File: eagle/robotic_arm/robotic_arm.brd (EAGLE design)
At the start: 160 x 100 mm, 0 parts

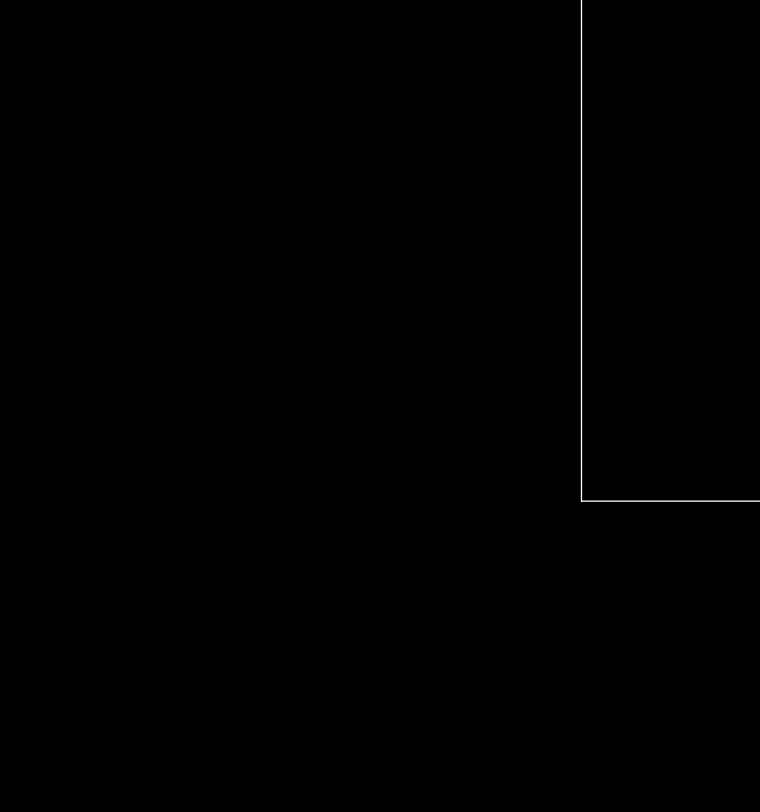
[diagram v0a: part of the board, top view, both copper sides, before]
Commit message: Added PWM driver and DEMUX to both robotic arm and touch glove.  Added some transistors to touch glove
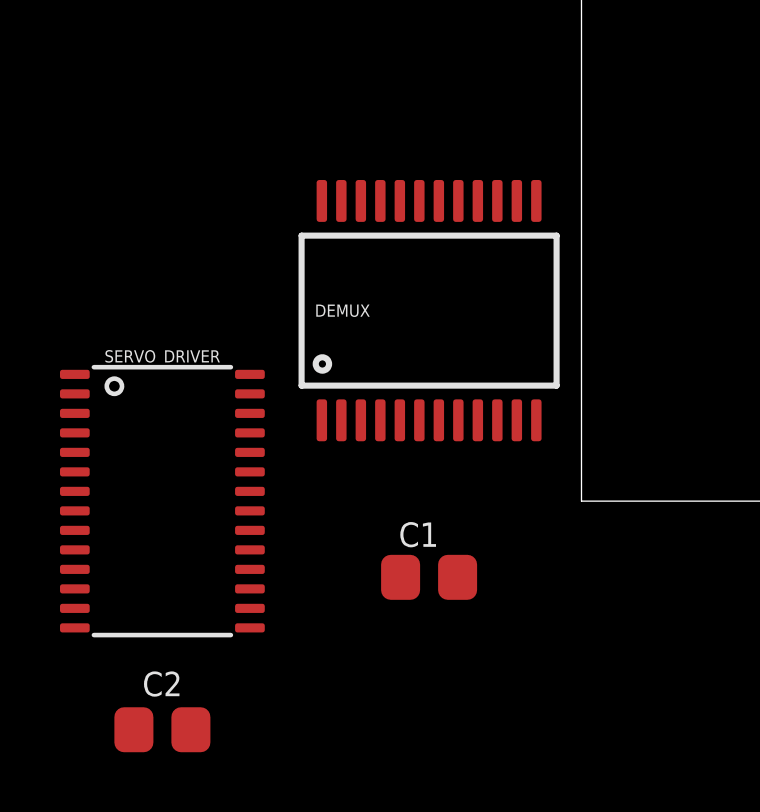
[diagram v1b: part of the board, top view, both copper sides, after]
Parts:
- added C1: CAP_CER_SMD-805_0.1UF-50V-10%, MrSwirlyEyes:CAP_CER_SMD-805_0.1UF-50V-10%
- added C2: CAP_CER_SMD-805_10UF-25V-10%, MrSwirlyEyes:CAP_CER_SMD-805_10UF-25V-10%
- added DEMUX: CD74HCT4067_16-CH_MUX-DEMUX, MrSwirlyEyes:SSOP24
- added SERVO_DRIVER: PCA9685_16-CH_12-BIT_PWM-DRIVER, MrSwirlyEyes:TSSOP28
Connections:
- new net C10: DEMUX.22
- new net C5: DEMUX.4
- new net C6: DEMUX.3
- new net C7: DEMUX.2
- new net C8: DEMUX.23
- new net FORCE_1: DEMUX.9
- new net FORCE_2: DEMUX.8
- new net FORCE_3: DEMUX.7
- new net FORCE_4: DEMUX.6
- new net FORCE_5: DEMUX.5
- new net GND: C1.2, C2.2, DEMUX.12, DEMUX.15, SERVO_DRIVER.1, SERVO_DRIVER.14, SERVO_DRIVER.2, SERVO_DRIVER.23, SERVO_DRIVER.24, SERVO_DRIVER.25, SERVO_DRIVER.3, SERVO_DRIVER.4, SERVO_DRIVER.5
- new net N$16: DEMUX.21
- new net N$19: SERVO_DRIVER.11
- new net N$20: SERVO_DRIVER.12
- new net N$21: SERVO_DRIVER.13
- new net N$22: SERVO_DRIVER.15
- new net N$23: SERVO_DRIVER.16
- new net N$24: SERVO_DRIVER.17
- new net N$25: SERVO_DRIVER.18
- new net N$26: SERVO_DRIVER.19
- new net N$27: SERVO_DRIVER.20
- new net N$28: SERVO_DRIVER.21
- new net N$29: SERVO_DRIVER.22
- new net S0: DEMUX.10
- new net S1: DEMUX.11
- new net S2: DEMUX.14
- new net S3: DEMUX.13
- new net SCL: SERVO_DRIVER.26
- new net SDA: SERVO_DRIVER.27
- new net SERVO_INDEX: SERVO_DRIVER.9
- new net SERVO_MIDDLE: SERVO_DRIVER.8
- new net SERVO_PINKY: SERVO_DRIVER.6
- new net SERVO_RING: SERVO_DRIVER.7
- new net SERVO_THUMB: SERVO_DRIVER.10
- new net SIG: DEMUX.1
- new net TEMP_1: DEMUX.20
- new net TEMP_2: DEMUX.19
- new net TEMP_3: DEMUX.18
- new net TEMP_4: DEMUX.17
- new net TEMP_5: DEMUX.16
- new net VCC: C1.1, C2.1, DEMUX.24, SERVO_DRIVER.28

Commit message: Added vibe motor plus transistor driver arrangement
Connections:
- net N$19 renamed PWM5
- net N$20 renamed PWM6
- net N$21 renamed PWM7
- net N$22 renamed PWM8
- net N$23 renamed PWM9
- net N$24 renamed PWM10
- net N$25 renamed PWM11
- net N$26 renamed PWM12
- net N$27 renamed PWM13
- net N$28 renamed PWM14
- net N$29 renamed PWM15
- removed net N$16: DEMUX.21
- new net C9: DEMUX.22
- net C10: now also DEMUX.21; no longer DEMUX.22
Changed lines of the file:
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@@
 <contactref element="DEMUX" pad="23"/>
 </signal>
-<signal name="C10">
+<signal name="C9">
 <contactref element="DEMUX" pad="22"/>
 </signal>
-<signal name="N$16">
+<signal name="C10">
 <contactref element="DEMUX" pad="21"/>
 </signal>
@@
 <contactref element="SERVO_DRIVER" pad="10"/>
 </signal>
-<signal name="N$19">
+<signal name="PWM5">
 <contactref element="SERVO_DRIVER" pad="11"/>
 </signal>
-<signal name="N$20">
+<signal name="PWM6">
 <contactref element="SERVO_DRIVER" pad="12"/>
 </signal>
-<signal name="N$21">
+<signal name="PWM7">
 <contactref element="SERVO_DRIVER" pad="13"/>
 </signal>
-<signal name="N$22">
+<signal name="PWM8">
 <contactref element="SERVO_DRIVER" pad="15"/>
 </signal>
-<signal name="N$23">
+<signal name="PWM9">
 <contactref element="SERVO_DRIVER" pad="16"/>
 </signal>
-<signal name="N$24">
+<signal name="PWM10">
 <contactref element="SERVO_DRIVER" pad="17"/>
 </signal>
-<signal name="N$25">
+<signal name="PWM11">
 <contactref element="SERVO_DRIVER" pad="18"/>
 </signal>
-<signal name="N$26">
+<signal name="PWM12">
 <contactref element="SERVO_DRIVER" pad="19"/>
 </signal>
-<signal name="N$27">
+<signal name="PWM13">
 <contactref element="SERVO_DRIVER" pad="20"/>
 </signal>
-<signal name="N$28">
+<signal name="PWM14">
 <contactref element="SERVO_DRIVER" pad="21"/>
 </signal>
-<signal name="N$29">
+<signal name="PWM15">
 <contactref element="SERVO_DRIVER" pad="22"/>
 </signal>

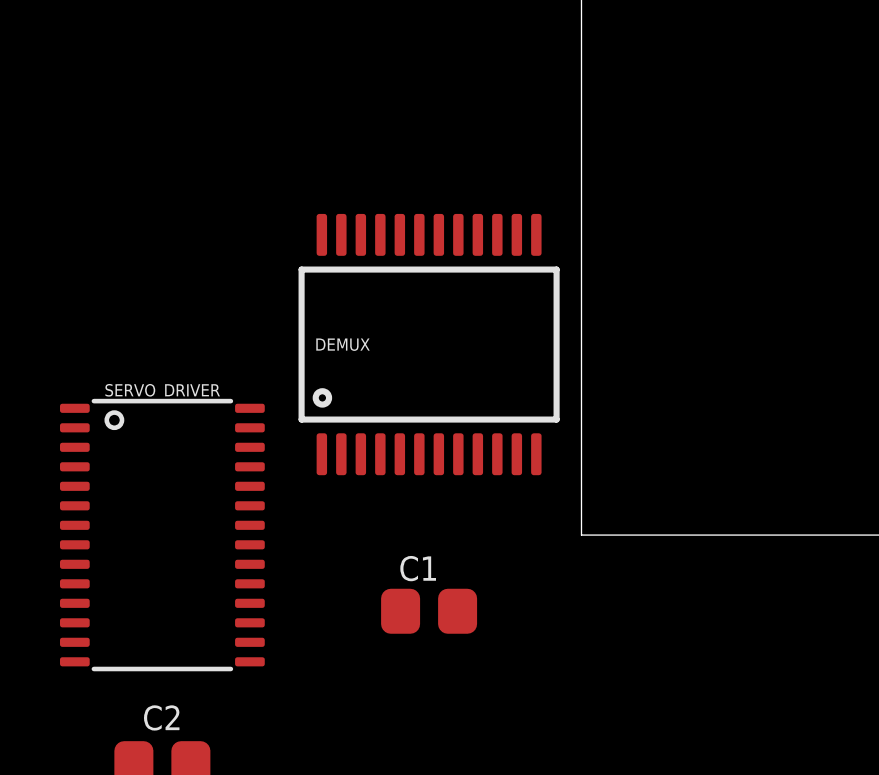
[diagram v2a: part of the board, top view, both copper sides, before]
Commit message: Added Peltier driving circuitry
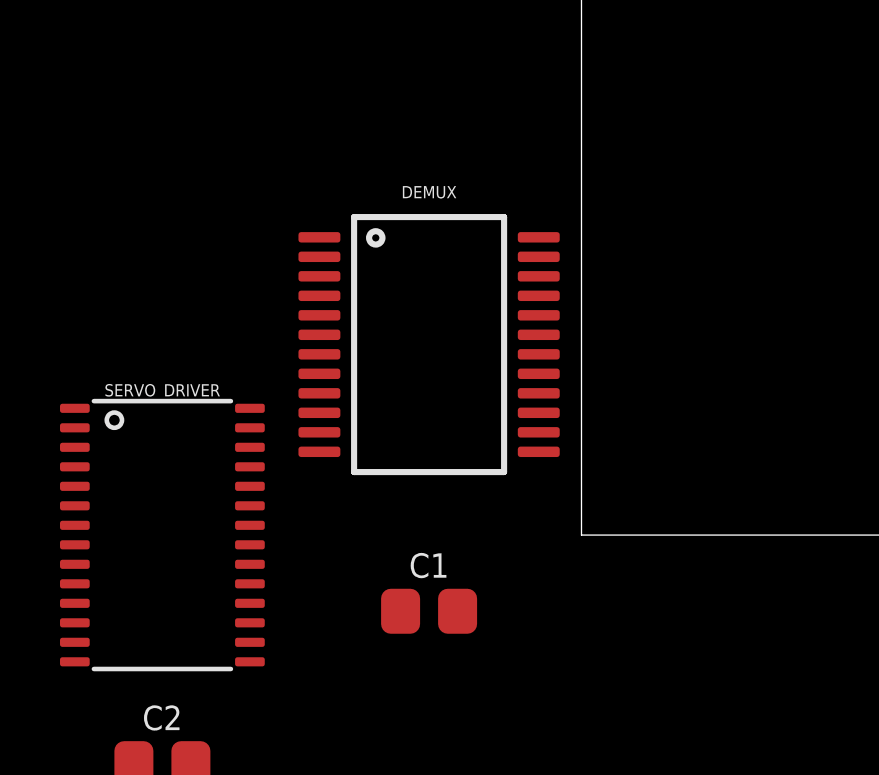
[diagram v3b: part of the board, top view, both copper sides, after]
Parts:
- DEMUX: value CD74HCT4067_16-CH_MUX-DEMUX -> CD74HC4067-SM96_16:1_MUX-DEMUX
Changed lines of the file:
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@@
 </autorouter>
 <elements>
-<element name="DEMUX" library="MrSwirlyEyes" package="SSOP24" value="CD74HCT4067_16-CH_MUX-DEMUX" x="-5.08" y="6.35">
+<element name="DEMUX" library="MrSwirlyEyes" package="SSOP24" value="CD74HC4067-SM96_16:1_MUX-DEMUX" x="-5.08" y="6.35">
 <attribute name="CREATOR" value="MrSwirlyEyes" x="-5.08" y="6.35" size="1.778" layer="27" display="off"/>
-<attribute name="DATASHEET" value="http://www.ti.com/lit/ds/symlink/cd74hct4067-q1.pdf" x="-5.08" y="6.35" size="1.778" layer="27" display="off"/>
+<attribute name="DATASHEET" value="http://www.ti.com/lit/ds/symlink/cd74hc4067.pdf" x="-5.08" y="6.35" size="1.778" layer="27" display="off"/>
 <attribute name="DIST" value="Digikey" x="-5.08" y="6.35" size="1.778" layer="27" display="off"/>
-<attribute name="DISTPN" value="296-37976-1-ND" x="-5.08" y="6.35" size="1.778" layer="27" display="off"/>
+<attribute name="DISTPN" value="296-9226-1-ND" x="-5.08" y="6.35" size="1.778" layer="27" display="off"/>
 <attribute name="MFR" value="Texas Instruments" x="-5.08" y="6.35" size="1.778" layer="27" display="off"/>
-<attribute name="MPN" value="CD74HCT4067QM96Q1" x="-5.08" y="6.35" size="1.778" layer="27" display="off"/>
+<attribute name="MPN" value="CD74HC4067SM96" x="-5.08" y="6.35" size="1.778" layer="27" display="off"/>
 <attribute name="TESTED" value="NO" x="-5.08" y="6.35" size="1.778" layer="27" display="off"/>
 </element>
@@
 <wire x1="-11.0522" y1="0.975" x2="-11.0522" y2="1.625" width="0" layer="19" extent="1-1"/>
 <wire x1="-4.13" y1="-2.54" x2="-11.0522" y2="0.975" width="0" layer="19" extent="1-1"/>
-<wire x1="-1.505" y1="2.694" x2="-4.13" y2="-2.54" width="0" layer="19" extent="1-1"/>
-<wire x1="-2.805" y1="10.006" x2="-1.505" y2="2.694" width="0" layer="19" extent="1-1"/>
+<wire x1="-8.736" y1="2.775" x2="-4.13" y2="-2.54" width="0" layer="19" extent="1-1"/>
+<wire x1="-1.424" y1="4.075" x2="-8.736" y2="2.775" width="0" layer="19" extent="1-1"/>
 </signal>
 <signal name="VCC">
@@
 <wire x1="-6.03" y1="-2.54" x2="-14.92" y2="-7.62" width="0" layer="19" extent="1-1"/>
 <wire x1="-11.0522" y1="4.225" x2="-6.03" y2="-2.54" width="0" layer="19" extent="1-1"/>
-<wire x1="-8.655" y1="10.006" x2="-11.0522" y2="4.225" width="0" layer="19" extent="1-1"/>
+<wire x1="-1.424" y1="9.925" x2="-11.0522" y2="4.225" width="0" layer="19" extent="1-1"/>
 </signal>
 <signal name="S0">

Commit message: Added FSR driver and servo driver for robotic arm
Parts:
- added A1, A2, A3, A4, A5: TMP36, MrSwirlyEyes:CONNECTOR_TMP36
- added C10, C12, C14, C16, C3, C4, C5, C6, C7, C8: CAP_CER_SMD-805_0.1UF-50V-10%, MrSwirlyEyes:CAP_CER_SMD-805_0.1UF-50V-10%
- added C11, C13, C15, C17, C9: CAP_POL_ALUM-ELECTROLYTIC_SMD_100UF-16V-20%, MrSwirlyEyes:CAP_POL_ALUM-ELECTROLYTIC_100UF-16V-20%_6.3LW-6.10H
- added F1, F2, F3, F4, F5: FSR, MrSwirlyEyes:CONNECTOR_FSR
- added R1, R2, R3, R4, R5: RES_SMD-805_10K-5%-1/8W, MrSwirlyEyes:RES_SMD-805_10K-5%-1/8W
- added S1, S2, S3, S4, S5: SERVO, MrSwirlyEyes:CONNECTOR_SERVO
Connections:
- net FORCE_1: now also F1.-, F2.-, F3.-, F4.-, F5.-, R1.2, R2.2, R3.2, R4.2, R5.2
- net GND: now also A1.3, A2.3, A3.3, A4.3, A5.3, C10.2, C11.K, C12.2, C13.K, C14.2, C15.K, C16.2, C17.K, C3.2, C4.2, C5.2, C6.2, C7.2, C8.2, C9.K, R1.1, R2.1, R3.1, R4.1, R5.1, S1.3, S2.3, S3.3, S4.3, S5.3
- net SERVO_INDEX: now also S4.1
- net SERVO_MIDDLE: now also S3.1
- net SERVO_PINKY: now also S1.1
- net SERVO_RING: now also S2.1
- net SERVO_THUMB: now also S5.1
- net TEMP_1: now also A1.2
- net TEMP_2: now also A2.2
- net TEMP_3: now also A3.2
- net TEMP_4: now also A4.2
- net TEMP_5: now also A5.2
- net VCC: now also A1.1, A2.1, A3.1, A4.1, A5.1, C10.1, C11.A, C12.1, C13.A, C14.1, C15.A, C16.1, C17.A, C3.1, C4.1, C5.1, C6.1, C7.1, C8.1, C9.A, F1.+, F2.+, F3.+, F4.+, F5.+, S1.2, S2.2, S3.2, S4.2, S5.2

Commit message: Modfied git ignore.  Added h bridge files.  Modified EAGLE files
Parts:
- C1, C10, C12, C14, C16, C3, C4, C5, C6, C7, C8: value CAP_CER_SMD-805_0.1UF-50V-10% -> 0.1uF/50V; device MrSwirlyEyes:CAP_CER_SMD-805_0.1UF-50V-10% -> MrSwirlyEyes:CAP_CER_SMD-805
- C11, C13, C15, C17, C9: value CAP_POL_ALUM-ELECTROLYTIC_SMD_100UF-16V-20% -> 100UF/16V; device MrSwirlyEyes:CAP_POL_ALUM-ELECTROLYTIC_100UF-16V-20%_6.3LW-6.10H -> MrSwirlyEyes:CAP_POL_ALUM-ELECTROLYTIC
- C2: value CAP_CER_SMD-805_10UF-25V-10% -> 10uF/25V; device MrSwirlyEyes:CAP_CER_SMD-805_10UF-25V-10% -> MrSwirlyEyes:CAP_CER_SMD-805
- DEMUX: value CD74HC4067-SM96_16:1_MUX-DEMUX -> CH16_MUX-DEMUX; device MrSwirlyEyes:SSOP24 -> MrSwirlyEyes:SSOP-24
- R1, R2, R3, R4, R5: value RES_SMD-805_10K-5%-1/8W -> 10KΩ; device MrSwirlyEyes:RES_SMD-805_10K-5%-1/8W -> MrSwirlyEyes:RESC2012X60_HS
- S1, S2, S3, S4, S5: value SERVO -> HK15298B
- SERVO_DRIVER: value PCA9685_16-CH_12-BIT_PWM-DRIVER -> PCA9685; device MrSwirlyEyes:TSSOP28 -> MrSwirlyEyes:TSSOP-28
- moved C7 271.5 mm to (-36.8, -405.1)
- moved F1 271.4 mm to (-29.2, -416.6)
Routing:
- net VCC: track 0.00 -> 31.5 mm

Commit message: Rev 1 of Robotic Arm schematic complete
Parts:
- removed DEMUX: CH16_MUX-DEMUX, MrSwirlyEyes:SSOP-24
- removed F1, F2, F3, F4, F5: FSR, MrSwirlyEyes:CONNECTOR_FSR
- removed R1, R2, R3, R4, R5: 10KΩ, MrSwirlyEyes:RESC2012X60_HS
- removed SERVO_DRIVER: PCA9685, MrSwirlyEyes:TSSOP-28
- added A6: ANTENNASMD5, lib_kenmei:ANTENNA-CHIP5
- added B1: 748421245, lib_kenmei:0805_BALUN
- added BATT1: BATTERYPTH_HOLES, MrSwirlyEyes:DUAL_PTH_PADS
- added C18, C25, C82, C92, C94, C95, C97: 10uF/25V, MrSwirlyEyes:CAP_CER_SMD-805
- added C19, C26, C47, C48, C49, C50, C51, C52, C54, C56, C63, C79, C81, C83, C93, C96, C98: 0.1uF/50V, MrSwirlyEyes:CAP_CER_SMD-805
- added C20: 1000uF/50V, MrSwirlyEyes:CAP_POL_DIA12.5-LS5-H27
- added C53, C55, C57, C58, C64, C85: 1uF/25V, MrSwirlyEyes:CAP_CER_SMD-805
- added C59, C60: 12pF/250V, MrSwirlyEyes:CAP_CER_SMD-805
- added C61: 22PF/250V, MrSwirlyEyes:CAP_CER_SMD-805
- added C62: 0.75PF/100V, MrSwirlyEyes:CAP_CER_SMD-805
- added C80: 220uF/16V, MrSwirlyEyes:CAP_POL_SMD_L6.6-W6.6
- added C84: 100UF/16V, MrSwirlyEyes:CAP_POL_SMD_L6.6-W6.6
- added D6, D7: 1A/50V, MrSwirlyEyes:DIODE_SMD_1A-50V-SOD123F
- added DEMUX1: CH16_MUX-DEMUX, MrSwirlyEyes:SSOP-24
- added FSR1, FSR2, FSR3, FSR4, FSR5: FSR, MrSwirlyEyes:CONNECTOR_FSR
- added J1: (no value), MrSwirlyEyes:2X3-NS
- added J2: (ID,OD)=(2.1,5.5)MM, MrSwirlyEyes:POWER_JACK_SLOT_ID2.1MM-OD5.5MM
- added JP1: FTDIPTH-RA, MrSwirlyEyes:FTDI_BASIC-6PIN-MALE-RA
- added L1, L2: 10uH, MrSwirlyEyes:INDUCTOR_SMD-805
- added PWM_DRIVER: PCA9685, MrSwirlyEyes:TSSOP-28
- added R16, R39, R40, R41, R42, R43: 10KΩ, MrSwirlyEyes:RESISTOR_SMD-805
- added R17, R18: 4.7K, MrSwirlyEyes:RESISTOR_SMD-805
- added S6: HK15298B, MrSwirlyEyes:CONNECTOR_SERVO
- added SW1: 5A/28V, MrSwirlyEyes:SW-SLIDE_SPDT_5A-28V_13L-7W
- added U$1, U$2: NET_BRIDGE, MrSwirlyEyes:NET_BRIDGE
- added U6: ATMEGA128RFA1, MrSwirlyEyes:VFQFN-64
- added VREG1: 5A/5V, MrSwirlyEyes:TO-263-5
- added VREG3: 1A/3.3V, MrSwirlyEyes:SOIC-8_W3.9MM
- added Y1: 16MHz, MrSwirlyEyes:CRYSTAL-SMD-5X3
- C11, C13, C15, C17, C9: device MrSwirlyEyes:CAP_POL_ALUM-ELECTROLYTIC -> MrSwirlyEyes:CAP_POL_SMD_L6.6-W6.6
- C2: value 10uF/25V -> 100UF/16V; device MrSwirlyEyes:CAP_CER_SMD-805 -> MrSwirlyEyes:CAP_POL_SMD_L6.6-W6.6
- moved C1 687.5 mm to (-20.1, -689.9)
- moved C2 683.7 mm to (-31.2, -691.1)
- renumbered A1 to TEMP1, A2 to TEMP2, A3 to TEMP3, A4 to TEMP4, A5 to TEMP5
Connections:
- removed net FORCE_1: DEMUX.9, F1.-, F2.-, F3.-, F4.-, F5.-, R1.2, R2.2, R3.2, R4.2, R5.2
- removed net FORCE_2: DEMUX.8
- removed net FORCE_3: DEMUX.7
- removed net FORCE_4: DEMUX.6
- removed net FORCE_5: DEMUX.5
- removed net PWM5: SERVO_DRIVER.11
- removed net TEMP_1: DEMUX.20, TEMP1.2
- removed net TEMP_2: DEMUX.19, TEMP2.2
- removed net TEMP_3: DEMUX.18, TEMP3.2
- removed net TEMP_4: DEMUX.17, TEMP4.2
- removed net TEMP_5: DEMUX.16, TEMP5.2
- new net 3.3V: C83.1, C94.1, D7.A, VREG1.4
- new net 5V: C1.1, C10.1, C11.A, C12.1, C13.A, C14.1, C15.A, C16.1, C17.A, C2.A, C8.1, C9.A, S1.2, S2.2, S3.2, S4.2, S5.2, S6.2
- new net A0: U6.63
- new net A1: U6.64
- new net A2: U6.1
- new net A3: U6.2
- new net A4: U6.3
- new net A5: U6.4
- new net A6: U6.5
- new net A7: U6.6
- new net FSR_INDEX: DEMUX1.6, FSR4.-, R41.2
- new net FSR_MIDDLE: DEMUX1.7, FSR3.-, R40.2
- new net FSR_PINKY: DEMUX1.9, FSR1.-, R16.2
- new net FSR_RING: DEMUX1.8, FSR2.-, R39.2
- new net FSR_THUMB: DEMUX1.5, FSR5.-, R42.2
- new net MISO: J1.1, U6.39
- new net MOSI: J1.4, U6.38
- new net N$1: C20.+, C80.A, C81.1, C82.1, C84.A, C95.1, C96.1, C97.1, C98.1, D6.K, D7.K, SW1.P$1, VREG1.1, VREG1.2, VREG3.3, VREG3.4
- new net N$2: BATT1.-, J2.GND@2
- new net N$30: C60.1, U6.57, Y1.3
- new net N$32: B1.3, U6.9
- new net N$33: B1.4, U6.8
- new net N$34: B1.2, C61.1
- new net N$35: C59.1, U6.56, Y1.1
- new net N$38: L2.2, U$2.P$1
- new net N$39: A6.FEED, B1.1, C62.1
- new net N$41: C79.1, JP1.DTR
- new net N$42: JP1.CTS
- new net N$43: BATT1.+, J2.PWR, SW1.P$2
- new net NGND: C85.2, U$1.P$1, U$2.P$2
- new net PB4: U6.40
- new net PB5: U6.41
- new net PB6: U6.42
- new net PB7: U6.43
- new net PD4: U6.29
- new net PD5: U6.30
- new net PD6: U6.31
- new net PD7: U6.32
- new net PE2: U6.48
- new net PE3: U6.49
- new net PE4: U6.50
- new net PE5: U6.51
- new net PE6: U6.52
- new net PE7: U6.53
- new net PG0: U6.14
- new net PG1: U6.15
- new net PG2: U6.16
- new net PG3: U6.17
- new net PG4: U6.18
- new net PG5: U6.19
- new net RESET: C79.2, J1.5, R43.1, U6.12
- new net RX0: JP1.TXO, U6.46
- new net RX1: U6.27
- new net SCK: J1.3, U6.37
- new net SERVO_WRIST: PWM_DRIVER.11, S6.1
- new net SSN: U6.36
- new net TEMP_INDEX: DEMUX1.17, TEMP4.2
- new net TEMP_MIDDLE: DEMUX1.18, TEMP3.2
- new net TEMP_PINKY: DEMUX1.20, TEMP1.2
- new net TEMP_RING: DEMUX1.19, TEMP2.2
- new net TEMP_THUMB: DEMUX1.16, TEMP5.2
- new net TX0: JP1.RXI, U6.47
- new net TX1: U6.28
- net C10: now also DEMUX1.21; no longer DEMUX.21
- net C5: now also DEMUX1.4; no longer DEMUX.4
- net C6: now also DEMUX1.3; no longer DEMUX.3
- net C7: now also DEMUX1.2; no longer DEMUX.2
- net C8: now also DEMUX1.23; no longer DEMUX.23
- net C9: now also DEMUX1.22; no longer DEMUX.22
- net GND: now also B1.5, C18.2, C19.2, C2.K, C20.-, C25.2, C26.2, C47.2, C48.2, C49.2, C50.2, C51.2, C52.2, C53.2, C54.2, C55.2, C56.2, C57.2, C58.2, C59.2, C60.2, C61.2, C62.2, C63.2, C64.2, C80.K, C81.2, C82.2, C83.2, C84.K, C92.2, C93.2, C94.2, C95.2, C96.2, C97.2, C98.2, DEMUX1.12, DEMUX1.15, J1.6, J2.GND@1, JP1.GND, L2.1, PWM_DRIVER.1, PWM_DRIVER.14, PWM_DRIVER.2, PWM_DRIVER.23, PWM_DRIVER.24, PWM_DRIVER.25, PWM_DRIVER.3, PWM_DRIVER.4, PWM_DRIVER.5, R16.1, R39.1, R40.1, R41.1, R42.1, S6.3, U$1.P$2, U6.10, U6.11, U6.20, U6.24, U6.33, U6.35, U6.45, U6.55, U6.58, U6.61, U6.7, VREG1.3, VREG1.TAB, VREG3.1, VREG3.2; no longer C2.2, DEMUX.12, DEMUX.15, R1.1, R2.1, R3.1, R4.1, R5.1, SERVO_DRIVER.1, SERVO_DRIVER.14, SERVO_DRIVER.2, SERVO_DRIVER.23, SERVO_DRIVER.24, SERVO_DRIVER.25, SERVO_DRIVER.3, SERVO_DRIVER.4, SERVO_DRIVER.5
- net PWM10: now also PWM_DRIVER.17; no longer SERVO_DRIVER.17
- net PWM11: now also PWM_DRIVER.18; no longer SERVO_DRIVER.18
- net PWM12: now also PWM_DRIVER.19; no longer SERVO_DRIVER.19
- net PWM13: now also PWM_DRIVER.20; no longer SERVO_DRIVER.20
- net PWM14: now also PWM_DRIVER.21; no longer SERVO_DRIVER.21
- net PWM15: now also PWM_DRIVER.22; no longer SERVO_DRIVER.22
- net PWM6: now also PWM_DRIVER.12; no longer SERVO_DRIVER.12
- net PWM7: now also PWM_DRIVER.13; no longer SERVO_DRIVER.13
- net PWM8: now also PWM_DRIVER.15; no longer SERVO_DRIVER.15
- net PWM9: now also PWM_DRIVER.16; no longer SERVO_DRIVER.16
- net S0: now also DEMUX1.10; no longer DEMUX.10
- net S1: now also DEMUX1.11; no longer DEMUX.11
- net S2: now also DEMUX1.14; no longer DEMUX.14
- net S3: now also DEMUX1.13; no longer DEMUX.13
- net SCL: now also PWM_DRIVER.26, R17.1, U6.25; no longer SERVO_DRIVER.26
- net SDA: now also PWM_DRIVER.27, R18.1, U6.26; no longer SERVO_DRIVER.27
- net SERVO_INDEX: now also PWM_DRIVER.9; no longer SERVO_DRIVER.9
- net SERVO_MIDDLE: now also PWM_DRIVER.8; no longer SERVO_DRIVER.8
- net SERVO_PINKY: now also PWM_DRIVER.6; no longer SERVO_DRIVER.6
- net SERVO_RING: now also PWM_DRIVER.7; no longer SERVO_DRIVER.7
- net SERVO_THUMB: now also PWM_DRIVER.10; no longer SERVO_DRIVER.10
- net SIG: now also DEMUX1.1; no longer DEMUX.1
- net VCC: now also C18.1, C19.1, C25.1, C26.1, C47.1, C48.1, C49.1, C50.1, C51.1, C52.1, C53.1, C54.1, C55.1, C56.1, C57.1, C58.1, C63.1, C64.1, C85.1, C92.1, C93.1, D6.A, DEMUX1.24, FSR1.+, FSR2.+, FSR3.+, FSR4.+, FSR5.+, J1.2, JP1.VCC, L1.1, L1.2, PWM_DRIVER.28, R17.2, R18.2, R43.2, U6.21, U6.22, U6.23, U6.34, U6.44, U6.54, U6.59, U6.60, U6.62, VREG3.5, VREG3.6; no longer C1.1, C10.1, C11.A, C12.1, C13.A, C14.1, C15.A, C16.1, C17.A, C2.1, C8.1, C9.A, DEMUX.24, F1.+, F2.+, F3.+, F4.+, F5.+, S1.2, S2.2, S3.2, S4.2, S5.2, SERVO_DRIVER.28

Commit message: Rev 1:  Robotic Arm.  Added reset button to MCU.  Modified several of the component symbols.  Resized board
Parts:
- removed J1: (no value), MrSwirlyEyes:2X3-NS
- added AVR_ISP: AVR ISP, MrSwirlyEyes:2X3-NS
- added D1: 1A/50V, MrSwirlyEyes:DIODE_SMD_1A-50V-SOD123F
- added S7: TACTILE-SW_500mA/12V, MrSwirlyEyes:SW_MOMENTARY_SPST-NO_SMD_12V_50MA_5.2MM
- moved C1 742.0 mm to (-79.0, 49.8)
- moved C2 742.0 mm to (-90.2, 48.5)
- moved J2 742.0 mm to (-113.5, 55.1)
- moved VREG1 742.0 mm to (-105.2, 20.3)
- moved C20 742.0 mm to (-110.2, 37.3)
- moved S6 742.0 mm to (-86.9, 63.0)
- moved FSR1 672.4 mm to (-38.1, 89.7)
- moved FSR3 672.4 mm to (-38.1, 52.1)
- moved FSR2 672.4 mm to (-38.1, 70.9)
- moved FSR4 672.4 mm to (-38.1, 33.3)
- moved FSR5 672.4 mm to (-38.1, 14.5)
- moved A6 637.8 mm to (-210.1, 61.7)
- moved B1 637.8 mm to (-240.3, 35.8)
- moved C18 637.8 mm to (-207.8, 25.1)
- moved C19 637.8 mm to (-184.2, 36.6)
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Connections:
- net GND: now also AVR_ISP.6, S7.1; no longer J1.6
- net MISO: now also AVR_ISP.1; no longer J1.1
- net MOSI: now also AVR_ISP.4; no longer J1.4
- net RESET: now also AVR_ISP.5, D1.A, S7.3; no longer J1.5
- net SCK: now also AVR_ISP.3; no longer J1.3
- net VCC: now also AVR_ISP.2, D1.K; no longer J1.2
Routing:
- net VCC: track 31.5 -> 0.00 mm
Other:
- board size 160 x 100 mm -> 101.6 x 63.5 mm
- board text removed: "initializing robotic_arm"
